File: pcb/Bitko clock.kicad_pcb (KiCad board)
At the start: 2 copper layers, 101 x 64.1 mm, 15 parts

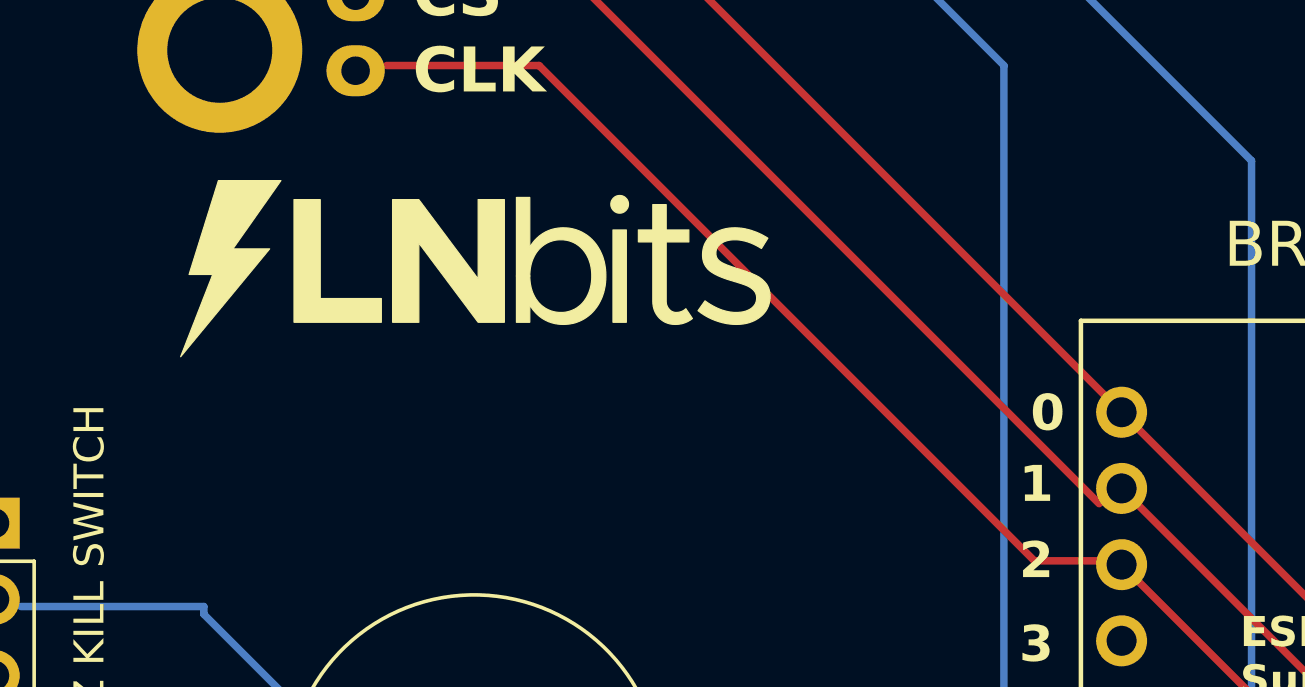
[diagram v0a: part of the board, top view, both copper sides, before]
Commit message: Working with serial output. neededd 5 sec boot delay
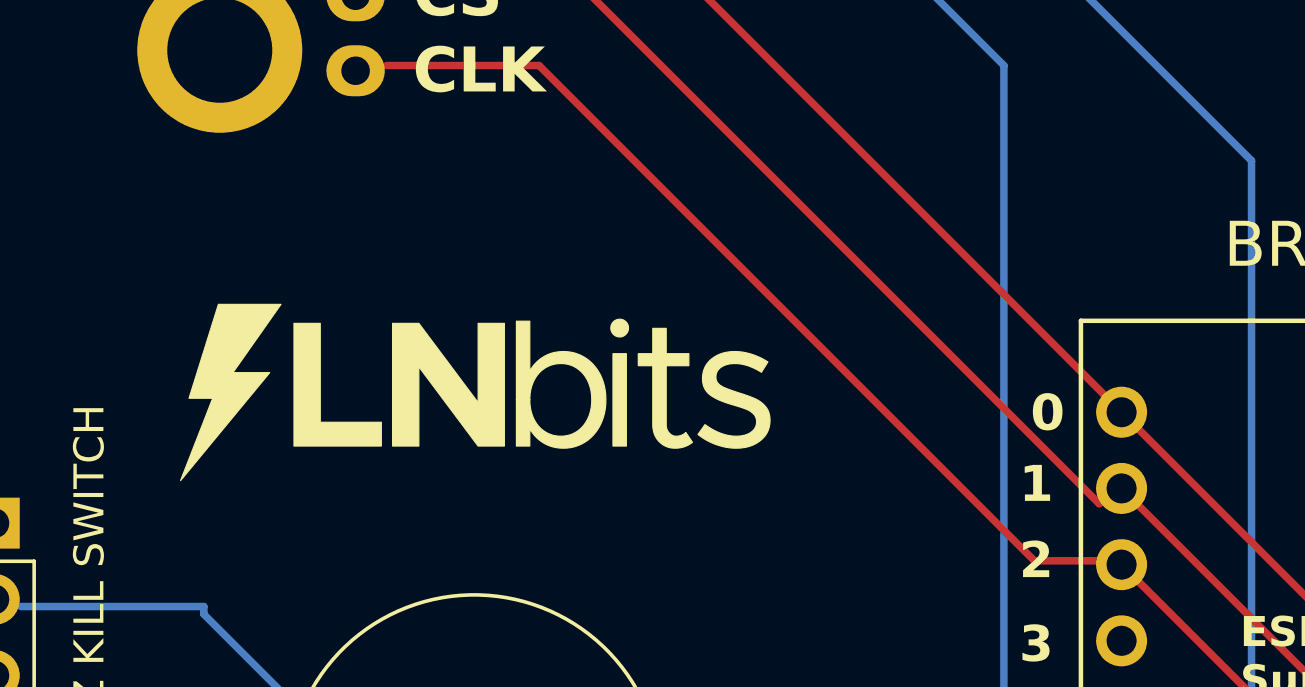
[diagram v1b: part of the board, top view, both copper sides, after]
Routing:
- net (no net): track 737.2 -> 738.1 mm

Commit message: Pin setup done!
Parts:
- moved REF** 4.00 mm to (81.2, 89.2)
- moved REF** 4.00 mm to (66.2, 89.2)
- moved BRRRR 2.16 mm to (47.1, 81.9)
- renumbered BZZZZ to BRRRR

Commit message: Added pins to PCB for reference
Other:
- board text added: "LED DIN 2 CS 5 CLK 4 BUZZER_PIN 20 TACTILE_SWITCH_PIN 10"
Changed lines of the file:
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@@
+    (effects (font (size 1.5 1.5) (thickness 0.3) bold) (justify left bottom))
+  )
+  (gr_text "LED\nDIN 2\nCS 5\nCLK 4 \n\nBUZZER_PIN 20\n\nTACTILE_SWITCH_PIN 10" (at 140.97 68.58) (layer "F.SilkS")
     (effects (font (size 1.5 1.5) (thickness 0.3) bold) (justify left bottom))
   )

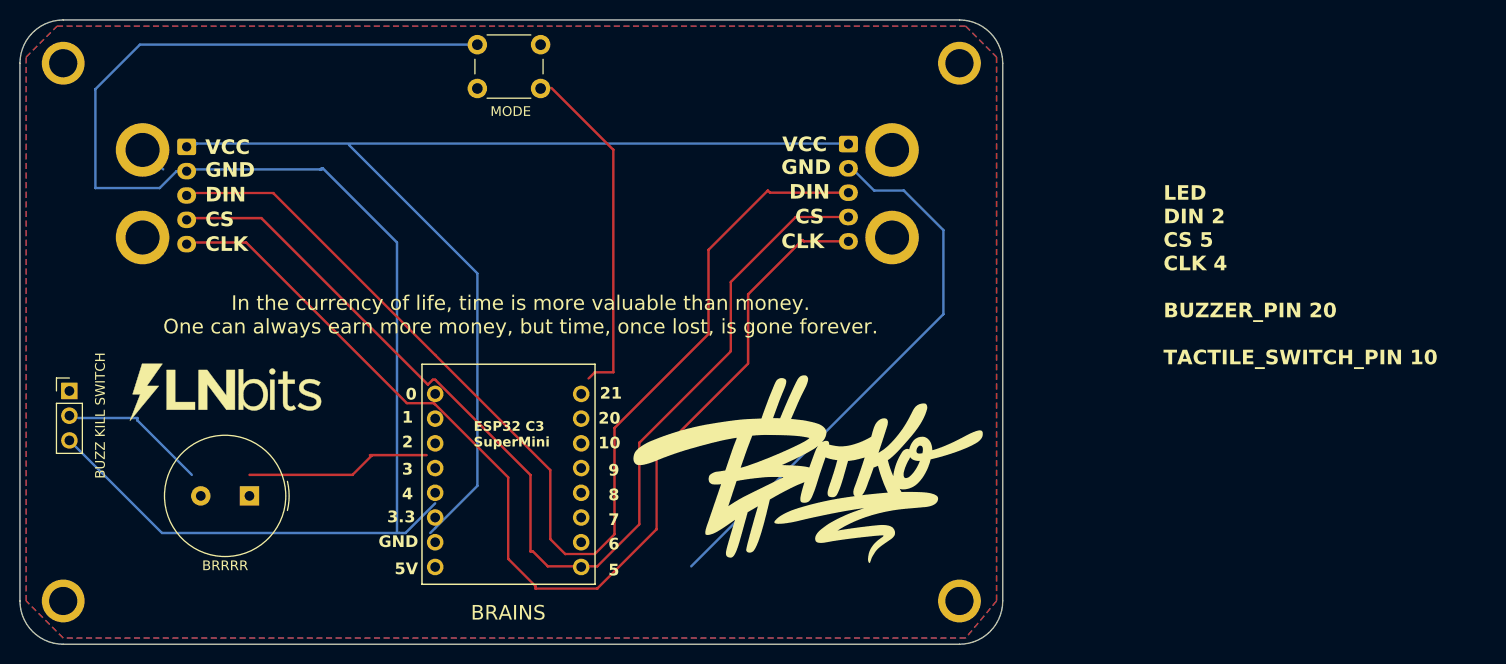
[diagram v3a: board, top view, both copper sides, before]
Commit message: Updated KiCad layout and tested component sizes
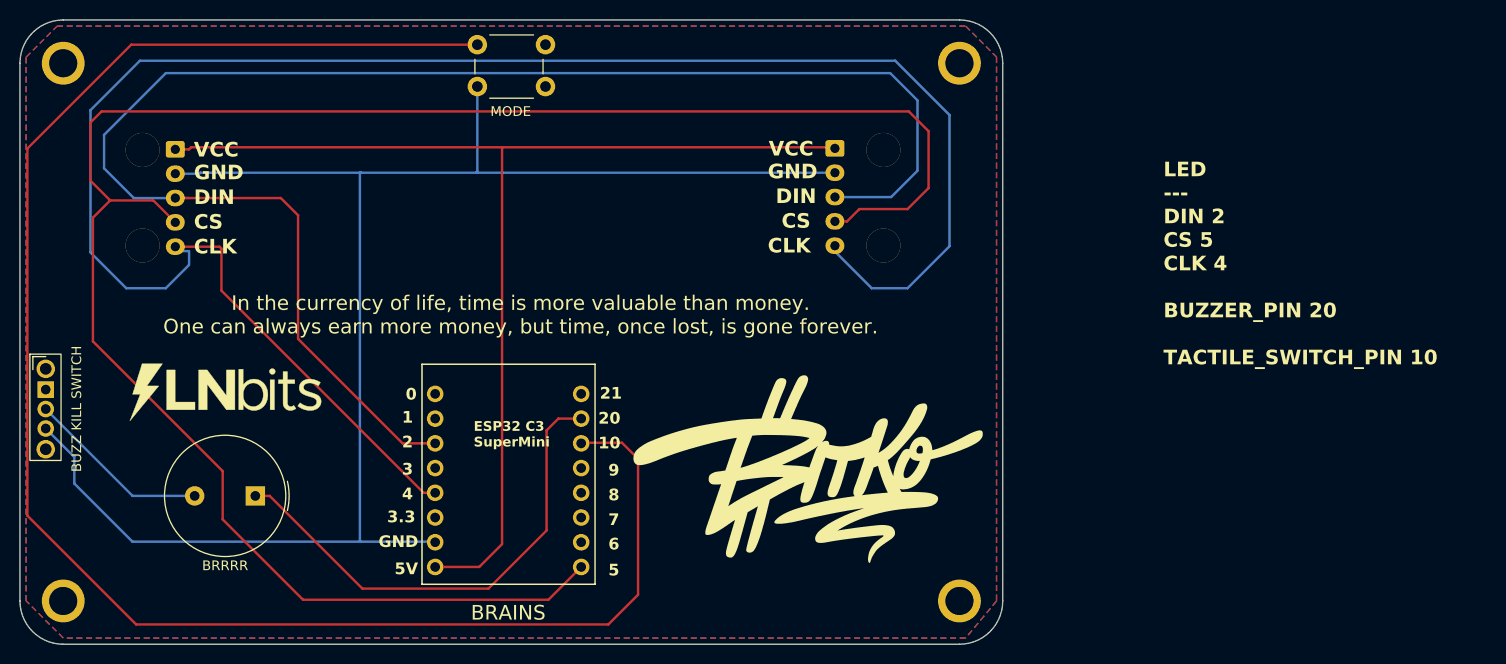
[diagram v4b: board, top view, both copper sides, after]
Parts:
- moved BUZZ KILL SWITCH 2.53 mm to (26.1, 70.5)
- moved JST_XH_B5B-XH-A_1x05 1.46 mm to (107.2, 46.2)
- moved ? 1.21 mm to (112.2, 56.2)
- moved JST_XH_B5B-XH-A_1x05 1.19 mm to (39.5, 46.3)
- moved REF** 0.89 mm to (112.2, 46.4)
- moved ? 0.82 mm to (36.1, 56.2)
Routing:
- net (no net): track 738.1 -> 1080.7 mm
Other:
- board text added: "LED --- DIN 2 CS 5 CLK 4 BUZZER_PIN 20 TACTILE_SWITCH_PIN 10"
- board text removed: "LED DIN 2 CS 5 CLK 4 BUZZER_PIN 20 TACTILE_SWITCH_PIN 10"

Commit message: PCB update. Added buzzer polarity, switch on/off and switch bitko logo for Bitcoin B
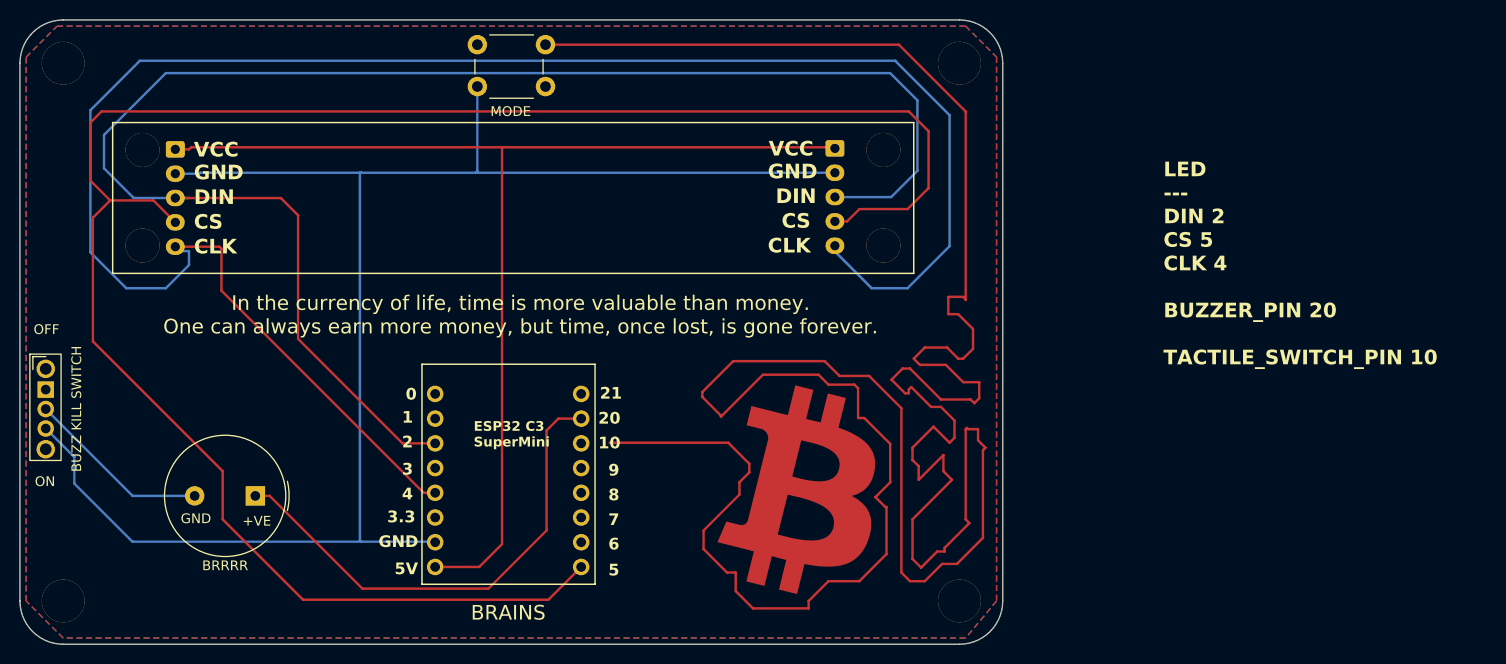
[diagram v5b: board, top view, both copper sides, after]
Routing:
- net (no net): track 1080.7 -> 1215.4 mm
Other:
- board text added: "+VE"
- board text added: "OFF"
- board text added: "ON"

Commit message: Connected unconnected track on PCB
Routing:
- net (no net): track 1215.4 -> 1218.4 mm
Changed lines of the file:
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@@
   (segment (start 118.745 66.675) (end 119.888 67.818) (width 0.25) (layer "F.Cu") (net 0))
   (segment (start 119.888 63.246) (end 118.872 63.246) (width 0.25) (layer "F.Cu") (net 0))
+  (segment (start 84.011 76.517) (end 81.153 76.517) (width 0.25) (layer "F.Cu") (net 0))
   (segment (start 112.395 83.058) (end 111.379 82.042) (width 0.25) (layer "F.Cu") (net 0))
   (segment (start 44.323 84.328) (end 52.578 92.583) (width 0.25) (layer "F.Cu") (net 0))
@@
   (segment (start 117.094 72.771) (end 115.062 70.739) (width 0.25) (layer "F.Cu") (net 0))
   (segment (start 99.822 69.469) (end 95.504 73.787) (width 0.25) (layer "F.Cu") (net 0))
+  (segment (start 84.074 76.454) (end 84.011 76.517) (width 0.25) (layer "F.Cu") (net 0))
   (segment (start 70.676 89.217) (end 66.153 89.217) (width 0.25) (layer "F.Cu") (net 0))
   (segment (start 109.728 52.451) (end 108.464 53.715) (width 0.25) (layer "F.Cu") (net 0))

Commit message: Updated pcb size and fixed minor issues
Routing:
- net (no net): track 1218.4 -> 1214.7 mm
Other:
- board size 101 x 64.1 mm -> 101 x 62.1 mm
